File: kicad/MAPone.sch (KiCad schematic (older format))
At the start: 27 parts, among them P1 CONN_1, P2 CONN_1, SW1 RST, U1 7805, U2 ATMEGA328-P, X1 16MHz

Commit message: MAPone schematic, work in progress
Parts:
- removed H3: Input, pin_strip_2, symbol CONN_2
- added J1: BARREL_JACK, symbol BARREL_JACK
- added J2: USB-Micro, symbol USB-Micro
- added P3, P4: CONN_1, vite_3mm, symbol CONN_1
- C1, C3, C4, C5, C6: footprint C2 -> Capacitors_ThroughHole:Capacitor7x2RM5
- C2: footprint CP_5x11mm -> Capacitors_ThroughHole:Capacitor5x6RM2.5
- D1: value D_CPL -> 1N4007; footprint (none) -> Diodes_ThroughHole:Diode_DO-35_SOD27_Horizontal_RM10
- D2, D3: footprint led_5mm_blue -> LEDs:LED-5MM
- H1, H5: footprint pin_strip_3 -> Pin_Headers:Pin_Header_Straight_1x03
- H2: footprint pin_strip_7 -> Pin_Headers:Pin_Header_Straight_1x07
- H4, H8: footprint pin_strip_6 -> Pin_Headers:Pin_Header_Straight_1x06
- H6, H7: footprint pin_strip_8 -> Pin_Headers:Pin_Header_Straight_1x08
- H9: footprint pin_strip_3x2 -> Pin_Headers:Pin_Header_Straight_2x03
- R1, R2, R3: footprint RC03 -> Resistors_ThroughHole:Resistor_Horizontal_RM10mm
- U1: footprint TO-220_Vertical -> Discret:LM78XXV
- U2: footprint dil_28-300_socket -> Sockets_DIP:DIP-28__300_ELL
- X1: footprint XTAL -> Crystals:Crystal_HC49-U_Vertical_3Pin
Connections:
- net GND: now also J1.2, J2.5 (GND), J2.T1, J2.T2, J2.T3, J2.T4, J2.T5, J2.T6; no longer P1.1, P2.1
- net V_USB: now also J2.1 (VBUS)
- net at D1.1 (Anode): now also J1.1
- no-connect marks 1 -> 10
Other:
- note added: "BLINK LED"
- note added: "MOUNT HOLES"
- note removed: "MOUNTING HOLES"
- moved on the sheet: D3, P1, P2, R3

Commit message: MAPone schematic, work in progress
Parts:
- added C7, C8: 22pF, Discret:C1, symbol C_CPL
- C2: footprint Capacitors_ThroughHole:Capacitor5x6RM2.5 -> Capacitors_Elko_ThroughHole:Elko_vert_11.2x6.3mm_RM2.5
- H7: footprint Pin_Headers:Pin_Header_Straight_1x08 -> Pin_Headers:Pin_Header_Straight_1x10
- H8: footprint Pin_Headers:Pin_Header_Straight_1x06 -> BADGEr:Header_FTDI
- H9: footprint Pin_Headers:Pin_Header_Straight_2x03 -> BADGEr:Header_ICSP
- J1: footprint (none) -> uControl:JACK_ALIM
- J2: footprint (none) -> BADGEr:USB_B_Micro
- P1, P2, P3, P4: footprint vite_3mm -> BADGEr:vite_3mm
- SW1: footprint SW_PB_V -> uControl:SW-PB
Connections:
- net GND: now also C7.2, C8.2
- net at U2.9 (PB6(XTAL1/TOSC1)), X1.1: now also C7.1
- net at U2.10 (PB7(XTAL2/TOSC2)), X1.2: now also C8.1
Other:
- moved on the sheet: C5, J2

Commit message: MAPone schematic, work in progress
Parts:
- added X?: ARDUINOSHIELD, symbol ARDUINOSHIELD
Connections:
- net 5V: now also X?.5V, X?.IORF (IOREF)
- net AD0: now also X?.AD0
- net AD1: now also X?.AD1
- net AD2: now also X?.AD2
- net AD3: now also X?.AD3
- net AD4_SDA: now also X?.AD4
- net AD5_SCL: now also X?.AD5
- net AREF: now also X?.AREF
- net GND: now also X?.GND1, X?.GND2, X?.GND3
- net MISO: now also X?.12
- net MOSI_P: now also X?.11
- net PB0: now also X?.8
- net PB1_P: now also X?.9
- net PD2: now also X?.2
- net PD3_P: now also X?.3
- net PD4: now also X?.4
- net PD5_P: now also X?.5
- net PD6_P: now also X?.6
- net PD7: now also X?.7
- net RST: now also X?.RST
- net RXD: now also X?.0
- net SCK: now also X?.13
- net SS_P: now also X?.10
- net TXD: now also X?.1
- net V_IN: now also X?.V_IN
- no-connect marks 10 -> 15
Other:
- moved on the sheet: J2
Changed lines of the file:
@@
 LIBS:power
 LIBS:CPL
+LIBS:arduino_shield
+LIBS:arduino_shieldsNCL
 LIBS:MAPone-cache
 EELAYER 25 0
@@
 10 84 01 40 0C B0 20 08 82 20 0C 00 62 80 05 41 10 04 61 00 10 03 2C 08 82 20 08 03 80 18 60 41
 10 04 41 18 00 C4 00 0B 82 20 08 C2 00 20 06 58 10 04 41 10 06 80 FF 05 00 29 65 D5 29 35 3D 11
-00 00 00 00 49 45 4E 44 AE 42 60 82 69
+00 00 00 00 49 45 4E 44 AE 42 60 82 39
 EndData
 $EndBitmap
@@
 L USB-Micro J2
 U 1 1 546F6B4E
-P 7675 4100
-F 0 "J2" H 7100 4025 60  0000 C CNN
-F 1 "USB-Micro" H 6950 4150 60  0000 C CNN
-F 2 "BADGEr:USB_B_Micro" H 7675 4100 60  0001 C CNN
-F 3 "" H 7675 4100 60  0000 C CNN
-	1    7675 4100
+P 9950 4100
+F 0 "J2" H 9375 4025 60  0000 C CNN
+F 1 "USB-Micro" H 9225 4150 60  0000 C CNN
+F 2 "BADGEr:USB_B_Micro" H 9950 4100 60  0001 C CNN
+F 3 "" H 9950 4100 60  0000 C CNN
+	1    9950 4100
 	1    0    0    -1
 $EndComp
@@
 NoConn ~ 4525 7200
 NoConn ~ 7225 1950
-NoConn ~ 7800 4175
-NoConn ~ 8225 3950
-NoConn ~ 8225 4100
-NoConn ~ 8225 4250
+NoConn ~ 10075 4175
+NoConn ~ 10500 3950
+NoConn ~ 10500 4100
+NoConn ~ 10500 4250
 Wire Wire Line
-	7375 4700 7375 4825
+	9650 4700 9650 4825
 Wire Wire Line
-	7375 4825 8675 4825
+	9650 4825 10950 4825
 Wire Wire Line
-	8675 4825 8675 3425
+	10950 4825 10950 3425
 Wire Wire Line
-	8675 3425 7375 3425
+	10950 3425 9650 3425
 Wire Wire Line
-	7375 3425 7375 3500
+	9650 3425 9650 3500
 Wire Wire Line
-	7525 3500 7525 3425
-Connection ~ 7525 3425
+	9800 3500 9800 3425
+Connection ~ 9800 3425
 Wire Wire Line
-	7525 4700 7525 4825
-Connection ~ 7525 4825
+	9800 4700 9800 4825
+Connection ~ 9800 4825
 Wire Wire Line
-	7675 4700 7675 4825
-Connection ~ 7675 4825
+	9950 4700 9950 4825
+Connection ~ 9950 4825
 Wire Wire Line
-	7825 4700 7825 4825
-Connection ~ 7825 4825
+	10100 4700 10100 4825
+Connection ~ 10100 4825
 Wire Wire Line
-	8225 4400 8300 4400
+	10500 4400 10575 4400
 Wire Wire Line
-	8300 4400 8300 4950
-Connection ~ 8300 4825
+	10575 4400 10575 4950
+Connection ~ 10575 4825
 $Comp
 L GND #PWR010
 U 1 1 546F85E6
-P 8300 4950
-F 0 "#PWR010" H 8300 4950 30  0001 C CNN
-F 1 "GND" H 8300 4880 30  0001 C CNN
-F 2 "" H 8300 4950 60  0000 C CNN
-F 3 "" H 8300 4950 60  0000 C CNN
-	1    8300 4950
+P 10575 4950
+F 0 "#PWR010" H 10575 4950 30  0001 C CNN
+F 1 "GND" H 10575 4880 30  0001 C CNN
+F 2 "" H 10575 4950 60  0000 C CNN
+F 3 "" H 10575 4950 60  0000 C CNN
+	1    10575 4950
 	1    0    0    -1
 $EndComp
-Text Label 8350 4825 0    47   ~ 0
+Text Label 10625 4825 0    47   ~ 0
 GND
 Wire Wire Line
-	8225 3800 8525 3800
-Text Label 8500 3800 2    40   ~ 0
+	10500 3800 10800 3800
+Text Label 10775 3800 2    40   ~ 0
 V_USB
 $Comp
@@
 L PWR_FLAG #FLG011
 U 1 1 54736205
-P 8525 3750
-F 0 "#FLG011" H 8525 4020 30  0001 C CNN
-F 1 "PWR_FLAG" H 8525 3980 30  0000 C CNN
-F 2 "" H 8525 3750 60  0001 C CNN
-F 3 "" H 8525 3750 60  0001 C CNN
-	1    8525 3750
+P 10800 3750
+F 0 "#FLG011" H 10800 4020 30  0001 C CNN
+F 1 "PWR_FLAG" H 10800 3980 30  0000 C CNN
+F 2 "" H 10800 3750 60  0001 C CNN
+F 3 "" H 10800 3750 60  0001 C CNN
+	1    10800 3750
 	1    0    0    -1
 $EndComp
 Wire Wire Line
-	8525 3800 8525 3750
+	10800 3800 10800 3750
+$Comp
+L ARDUINOSHIELD X?
+U 1 1 5474B9FE
+P 7250 4375
+F 0 "X?" H 6900 5325 60  0000 C CNN
+F 1 "ARDUINOSHIELD" H 7250 4375 60  0000 C CNN
+F 2 "" H 7250 4375 60  0000 C CNN
+F 3 "" H 7250 4375 60  0000 C CNN
+	1    7250 4375
+	1    0    0    -1
+$EndComp
+Wire Wire Line
+	5900 3875 6300 3875
+Wire Wire Line
+	6300 3975 6050 3975
+Wire Wire Line
+	5900 4175 6300 4175
+Wire Wire Line
+	6300 4275 6050 4275
+Wire Wire Line
+	6300 4375 6050 4375
+Wire Wire Line
+	6300 4475 6050 4475
+Wire Wire Line
+	6300 4675 6050 4675
+Wire Wire Line
+	6300 4775 6050 4775
+Wire Wire Line
+	6300 4875 6050 4875
+Wire Wire Line
+	6300 4975 6050 4975
+Wire Wire Line
+	6300 5075 6050 5075
+Wire Wire Line
+	6300 5175 6050 5175
+Wire Wire Line
+	8450 4475 8200 4475
+Wire Wire Line
+	8450 4575 8200 4575
+Wire Wire Line
+	8450 4675 8200 4675
+Wire Wire Line
+	8450 4775 8200 4775
+Wire Wire Line
+	8450 4875 8200 4875
+Wire Wire Line
+	8450 4975 8200 4975
+Wire Wire Line
+	8450 5075 8200 5075
+Wire Wire Line
+	8450 5175 8200 5175
+Wire Wire Line
+	8450 3575 8200 3575
+Wire Wire Line
+	8450 3675 8200 3675
+Wire Wire Line
+	8450 3775 8200 3775
+Wire Wire Line
+	8450 3875 8200 3875
+Wire Wire Line
+	8450 3975 8200 3975
+Wire Wire Line
+	8450 4075 8200 4075
+Wire Wire Line
+	8450 4175 8200 4175
+Wire Wire Line
+	8450 4275 8200 4275
+Wire Wire Line
+	8450 3375 8200 3375
+Wire Wire Line
+	8450 3475 8200 3475
+Text Label 6050 4675 0    40   ~ 0
+AD0
+Text Label 6050 4775 0    40   ~ 0
+AD1
+Text Label 6050 4875 0    40   ~ 0
+AD2
+Text Label 6050 4975 0    40   ~ 0
+AD3
+Text Label 6050 5075 0    39   ~ 0
+AD4_SDA
+Text Label 6050 5175 0    40   ~ 0
+AD5_SCL
+Text Label 6050 4175 0    40   ~ 0
+5V
+Text Label 6050 4275 0    40   ~ 0
+GND
+Text Label 6050 4375 0    40   ~ 0
+GND
+Text Label 6050 4475 0    40   ~ 0
+V_IN
+Text Label 6050 3975 0    40   ~ 0
+RST
+Text Label 8450 3375 2    40   ~ 0
+AD5_SCL
+Text Label 8450 3475 2    40   ~ 0
+AD4_SDA
+Text Label 8450 3575 2    40   ~ 0
+AREF
+Text Label 8450 3675 2    40   ~ 0
+GND
+Text Label 8450 3775 2    40   ~ 0
+SCK
+Text Label 8450 3875 2    40   ~ 0
+MISO
+Text Label 8450 3975 2    40   ~ 0
+MOSI_P
+Text Label 8450 4075 2    40   ~ 0
+SS_P
+Text Label 8450 4175 2    40   ~ 0
+PB1_P
+Text Label 8450 4275 2    40   ~ 0
+PB0
+Text Label 8450 5175 2    39   ~ 0
+RXD
+Text Label 8450 5075 2    39   ~ 0
+TXD
+Text Label 8450 4975 2    40   ~ 0
+PD2
+Text Label 8450 4875 2    40   ~ 0
+PD3_P
+Text Label 8450 4775 2    40   ~ 0
+PD4
+Text Label 8450 4675 2    40   ~ 0
+PD5_P
+Text Label 8450 4575 2    40   ~ 0
+PD6_P
+Text Label 8450 4475 2    40   ~ 0
+PD7
+NoConn ~ 6800 5575
+NoConn ~ 7500 5575
+NoConn ~ 6300 3725
+NoConn ~ 6300 4075
+NoConn ~ 8200 3175
+Wire Wire Line
+	5900 4175 5900 3875
 $EndSCHEMATC

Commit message: MAPone PCB work in progress
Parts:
- removed X?: ARDUINOSHIELD, symbol ARDUINOSHIELD
- C1, C3, C4, C5, C6: footprint Capacitors_ThroughHole:Capacitor7x2RM5 -> Capacitors_SMD:C_0805_HandSoldering
- C7, C8: footprint Discret:C1 -> Capacitors_SMD:C_0805_HandSoldering
- D1: footprint Diodes_ThroughHole:Diode_DO-35_SOD27_Horizontal_RM10 -> Diodes_ThroughHole:Diode_DO-41_SOD81_Vertical_KathodeUp
- D2, D3: footprint LEDs:LED-5MM -> LEDs:LED-3MM
- H1: footprint Pin_Headers:Pin_Header_Straight_1x03 -> uControl:Header_3
- H2: footprint Pin_Headers:Pin_Header_Straight_1x07 -> Socket_Strips:Socket_Strip_Straight_1x06; symbol CONN_7 -> CONN_6
- H4: footprint Pin_Headers:Pin_Header_Straight_1x06 -> Socket_Strips:Socket_Strip_Straight_1x06
- H5: footprint Pin_Headers:Pin_Header_Straight_1x03 -> uControl:Header_A_REF
- H6: footprint Pin_Headers:Pin_Header_Straight_1x08 -> Socket_Strips:Socket_Strip_Straight_1x08
- H7: footprint Pin_Headers:Pin_Header_Straight_1x10 -> Socket_Strips:Socket_Strip_Straight_1x08; symbol CONN_10 -> CONN_8
- R1, R2, R3: footprint Resistors_ThroughHole:Resistor_Horizontal_RM10mm -> Resistors_SMD:R_0805_HandSoldering
- U2: footprint Sockets_DIP:DIP-28__300_ELL -> MAPone.pretty:DIP-28__300_ELL_ZIF
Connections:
- net 3V3: now also H2.2; no longer H2.3 (P3)
- net 5V: now also H2.3, H8.3; no longer H2.1 (P1), H2.4 (P4)
- net AD4_SDA: no longer H7.9
- net AD5_SCL: no longer H7.10
- net GND: now also H2.4; no longer H2.6 (P6)
- net RST: now also H2.1; no longer H2.2 (P2)
- net V_IN: now also H2.6; no longer H2.7 (P7)
- net V_USB: no longer H8.3
- no-connect marks 15 -> 10

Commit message: MAPone schematic/pcb complete
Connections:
- net VREF is gone; now on net AREF: C5.1, H5.2 (PM), U2.21 (AREF)
- net AREF: no longer H5.3 (P3), H7.8 (P8)
- new net Vext: H5.3 (P3), H7.8 (P8)
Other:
- note added: "NOTE : Vext = 5V MAX."
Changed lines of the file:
@@
 LIBS:power
 LIBS:CPL
-LIBS:arduino_shield
-LIBS:arduino_shieldsNCL
 LIBS:MAPone-cache
 EELAYER 25 0
@@
 00 11 60 41 10 04 41 18 00 44 80 05 41 10 04 61 00 10 01 16 04 41 10 84 01 40 04 58 10 04 41 10
 06 00 11 60 41 10 04 41 18 00 44 80 05 41 10 04 61 00 10 01 16 04 41 10 84 01 E0 7F 01 2F 14 66
-D9 0D DF 91 84 00 00 00 00 49 45 4E 44 AE 42 60 82 C5
+D9 0D DF 91 84 00 00 00 00 49 45 4E 44 AE 42 60 82 67
 EndData
 $EndBitmap
@@
 $EndComp
 Text Label 1525 2725 0    40   ~ 0
-VREF
-Text Label 1125 2500 0    40   ~ 0
 AREF
+Text Label 1125 2500 0    40   ~ 0
+Vext
 $Comp
 L CONN_3 H5
@@
 AD0
 Text Label 4425 4925 0    40   ~ 0
-AREF
+Vext
 Text Label 4425 4825 0    40   ~ 0
 GND
@@
 Wire Wire Line
 	10800 3800 10800 3750
+Text Notes 4450 5100 0    60   ~ 0
+NOTE : Vext = 5V MAX.
 $EndSCHEMATC

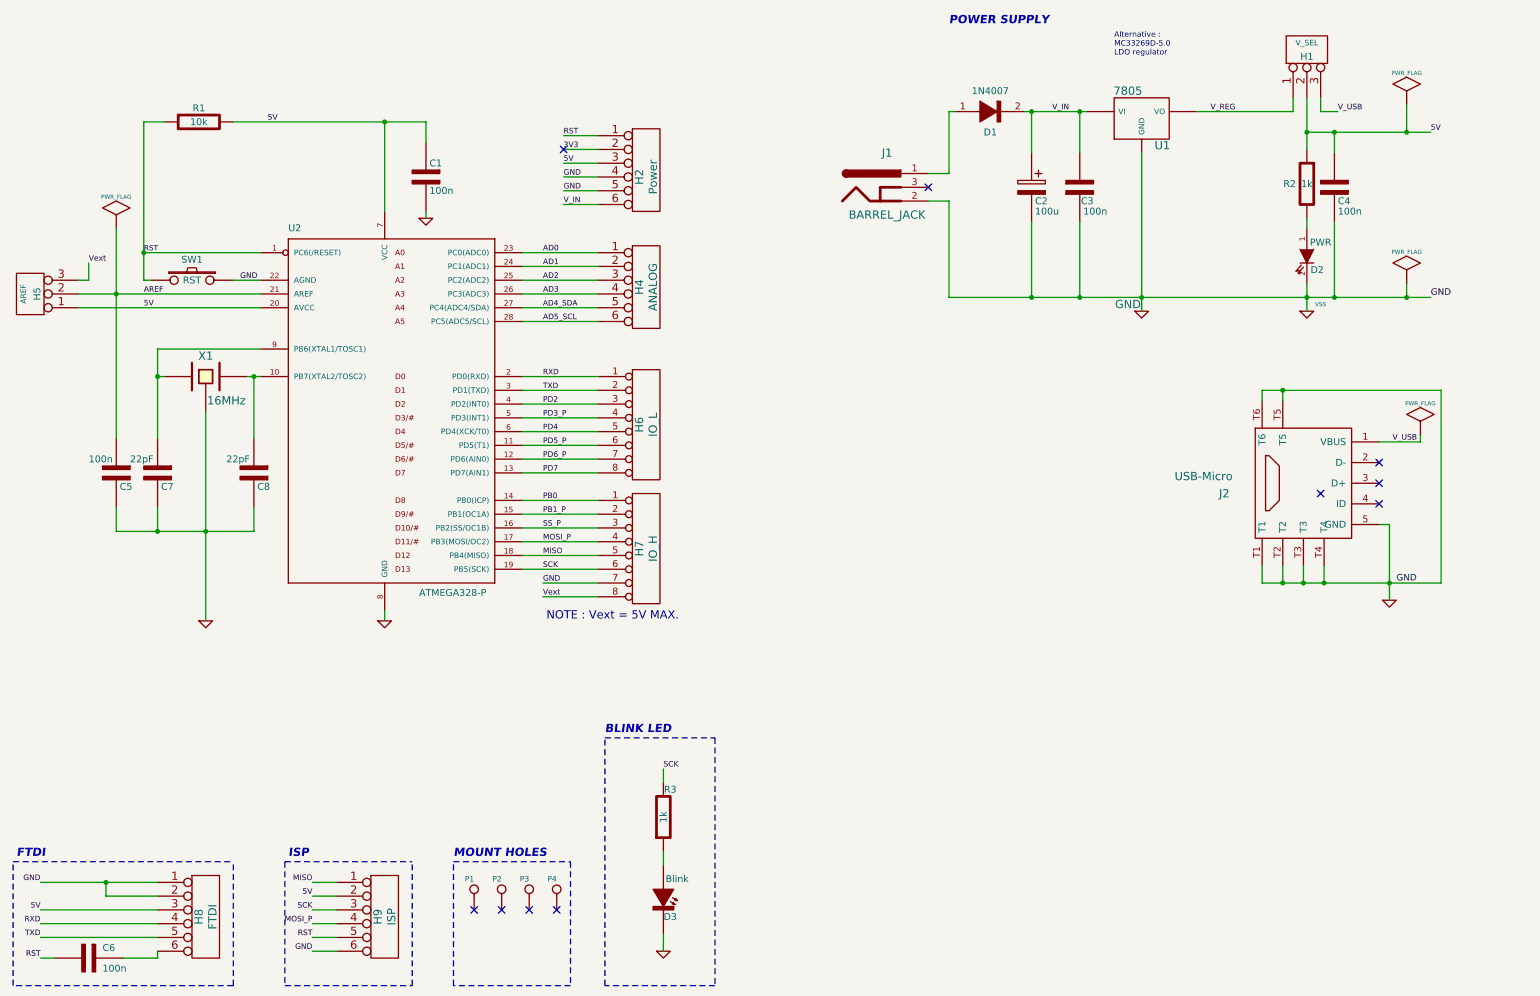
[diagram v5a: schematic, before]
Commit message: MAPone Schematic, PCB, BoM complete. USB<>UART PCB Pending
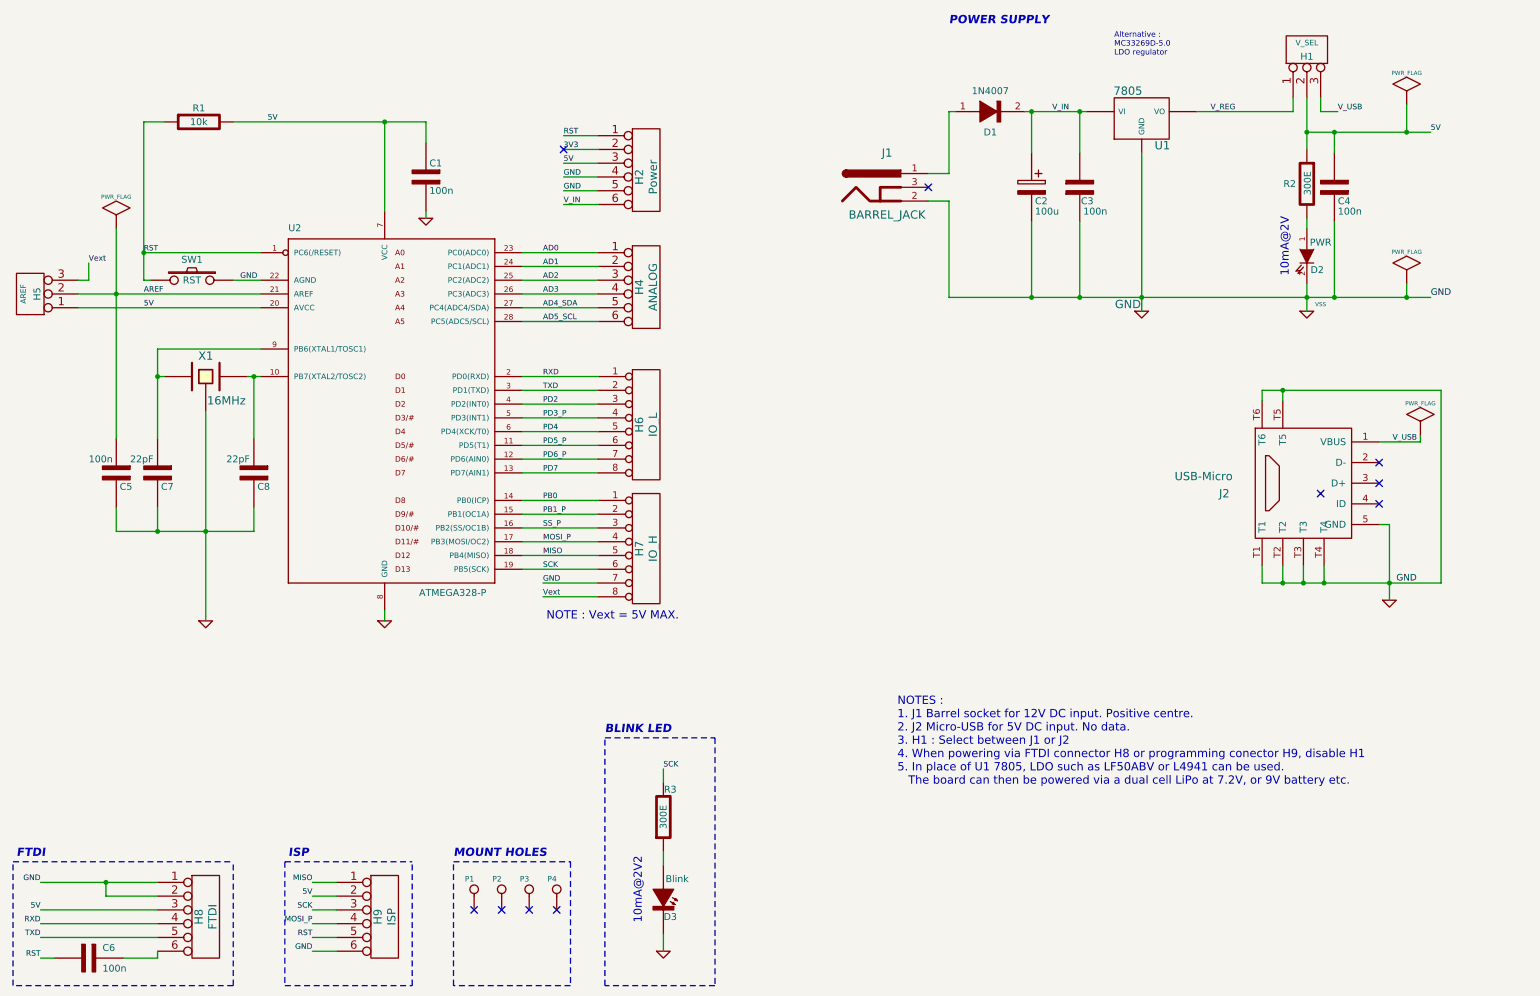
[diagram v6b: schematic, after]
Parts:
- R2, R3: value 1k -> 300E
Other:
- note added: "10mA@2V"
- note added: "10mA@2V2"
- note added: "NOTES :\n1. J1 Barrel socket for 12V DC input. Positive centre.\n2. J2 Micro-USB for 5V DC input. No data.\n3. H1 : Select between J1 or J2\n4. When powering via FTDI connector H8 or programming conector H9, disable H1\n5. In place of U1 7805, LDO such as LF50ABV or L4941 can be used. \n The board can then be powered via a dual cell LiPo at 7.2V, or 9V battery etc."
